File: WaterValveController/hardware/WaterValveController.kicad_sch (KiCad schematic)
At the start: 43 parts, among them J1 12V DC IN, J2 VALVE POWER, J3 RELAY MODULE, J4 FLOW SENSOR, J5 REMOTE RX, J6 ESP, K1 Relay module, SW1 MODE / CAL, U1 L7805 or R-78E5.0-1.0

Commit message: Switch remote to the RX480E logic-output receiver; add PCB prep parts
The 433 MHz receiver is an RX480E-4 module with 5 V logic outputs, not a
relay board. Firmware now defaults to active-high remote inputs. On the
board it plugs into a 7-pin socket powered from filtered 5 V (10R + 47uF
+ 100nF), with 1k series resistors and 100k pull-downs on D0-D3. The old
12 V screw terminal for the remote is gone.

Also adds a 100uF bulk capacitor at the relay header and four M3
mounting holes, renumbers the ESP header to J5 and the Nano decoupling
capacitor to C11, and drops the EasyEDA notes in favour of KiCad.

Co-Authored-By: Claude Opus 5.5 <noreply@anthropic.com>
Claude-Session: https://claude.ai/code/session_01AqRGusXgpSip5brBmMU9hY
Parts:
- removed C10, C12, C8: 100nF, Capacitor_THT:C_Disc_D5.0mm_W2.5mm_P5.00mm, symbol Device:C
- removed J5: REMOTE RX, TerminalBlock_Phoenix:TerminalBlock_Phoenix_MKDS-1,5-6-5.08_1x06_P5.08mm_Horizontal, symbol Connector:Screw_Terminal_01x06
- removed J6: ESP, Connector_PinHeader_2.54mm:PinHeader_1x03_P2.54mm_Vertical, symbol Connector_Generic:Conn_01x03
- removed RX1: 433 MHz 4-ch receiver (momentary), symbol WaterValve:RF_Receiver_4CH
- added C10: 100uF 16V, Capacitor_THT:CP_Radial_D6.3mm_P2.50mm, symbol Device:C_Polarized
- added C8: 47uF 16V, Capacitor_THT:CP_Radial_D5.0mm_P2.00mm, symbol Device:C_Polarized
- added H1, H2, H3, H4: M3, MountingHole:MountingHole_3.2mm_M3, symbol Mechanical:MountingHole
- added J5: ESP, Connector_PinHeader_2.54mm:PinHeader_1x03_P2.54mm_Vertical, symbol Connector_Generic:Conn_01x03
- added R13, R14, R15, R16: 100k, Resistor_THT:R_Axial_DIN0207_L6.3mm_D2.5mm_P10.16mm_Horizontal, symbol Device:R
- added R17: 10R, Resistor_THT:R_Axial_DIN0207_L6.3mm_D2.5mm_P10.16mm_Horizontal, symbol Device:R
- added U2: RX480E-4, Connector_PinSocket_2.54mm:PinSocket_1x07_P2.54mm_Vertical, symbol WaterValve:RX480E
- R10, R7, R8, R9: value 10k -> 1k
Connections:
- net +5V: now also C11.1, C10.1, J5.1 (Pin_1), R17.1; no longer R10.1, R7.1, R8.1, R9.1
- net ESP_DATA: now also J5.2 (Pin_2)
- net GND: now also C10.2, C8.2, J5.3 (Pin_3), R13.2, R14.2, R15.2, R16.2, U2.1 (GND)
- net RF1: now also R13.1
- net RF2: now also R14.1; no longer C9.1
- net RF3: now also R15.1
- net RF4: now also R16.1; no longer C11.1
- new net: C8.1, C9.1, R17.2, U2.2 (+V)
- new net RX_D0: R7.1, U2.3 (D0)
- new net RX_D1: R8.1, U2.4 (D1)
- new net RX_D2: R9.1, U2.5 (D2)
- new net RX_D3: R10.1, U2.6 (D3)
- no-connect marks 17 -> 18
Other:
- note added: "1. D2 flyback diode right at the valve terminals (stripe to +). 2. Valve current has its own pair (J2) back to J1: star ground at J1. 3. Decoupling: C1 + C2 on 12 V, C3 + C4 at U1, C10 at J3, C11 at the Nano, C6 at J4. 4. Flow input: R1 10k pull-up, R2 1k + C5 10nF filter, firmware glitch filter. 5. Button: R3 10k + C7 100nF. Remote: R7-R10 1k series, R13-R16 100k pull-downs, receiver supply filt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"
- note added: "J2: run the valve +12 V and return as their own pair, and keep them away from the sensor cable. Place J1 and J2 side by side. C10 sits at J3 to steady 5 V when the relay coil switches."
- note added: "MOUNTING HOLES (M3)"
- note added: "OFF-BOARD WIRING (connects to J2-J4; not placed on the PCB)"
- note added: "REMOTE RECEIVER (RX480E 433 MHz module, plugs into the board)"
- note added: "U2 plugs into a 7-pin socket. Check that the labels on the back of your module read GND, +V, D0, D1, D2, D3, VT in that order before ordering the PCB. Pair the remote in MOMENTARY mode. Keep the antenna clear of the relay, valve wires and metal."
- note removed: "1. D2 flyback diode right at the valve terminals (stripe to +). 2. Valve current has its own wire pair (J2) back to J1: star ground at J1. 3. Decoupling: C1 + C2 on 12 V, C3 + C4 at U1, C12 at the Nano, C6 at J4. 4. Flow input: R1 10k pull-up, R2 1k + C5 10nF filter, firmware glitch filter. 5. Button and remote inputs: 10k pull-ups + 100nF, firmware debounce. 6. F1 fuse + D1 crowbar protect again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"
- note removed: "J2: run the valve +12 V and return as their own pair, and keep them away from the sensor and remote cables."
- note removed: "OFF-BOARD WIRING (connects to J2-J5; these parts are not placed on the PCB)"
- note removed: "REMOTE RECEIVER INPUTS (433 MHz, 4 relay channels)"
- note removed: "Remote: all COM terminals to GND, NO1-NO4 to J5 pins 3-6. +12 V board shown; power a 5 V board from +5V instead."

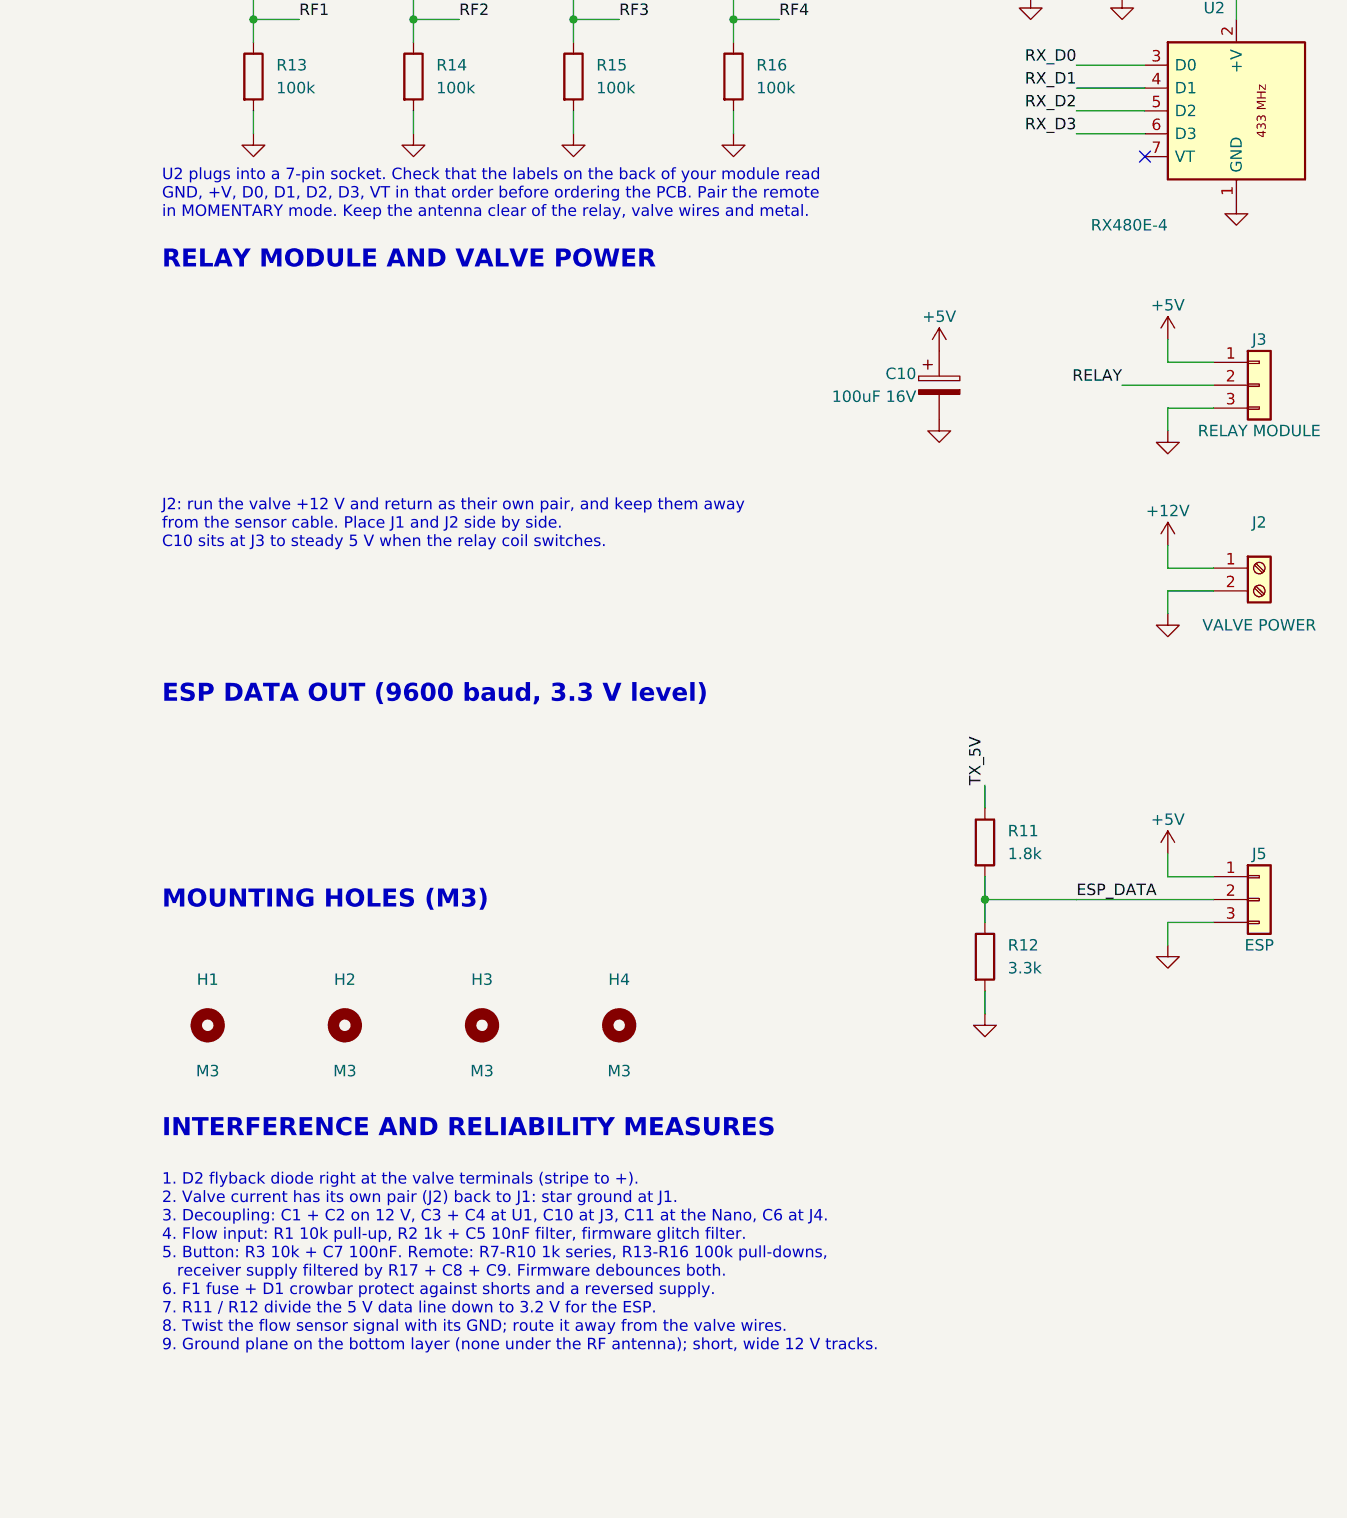
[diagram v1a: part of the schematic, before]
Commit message: Confirm RX480E pin order and mark socket orientation
The module's back labels (RX480R_4CH V4) run GND, +V, D0, D1, D2, D3, VT
from the learn-button end to the antenna end, matching the U2 socket.
Notes now say to mark both socket ends on the silkscreen, since the
upright module would also fit backwards, and the antenna advice covers
an upright module.

Co-Authored-By: Claude Opus 5.5 <noreply@anthropic.com>
Claude-Session: https://claude.ai/code/session_01AqRGusXgpSip5brBmMU9hY
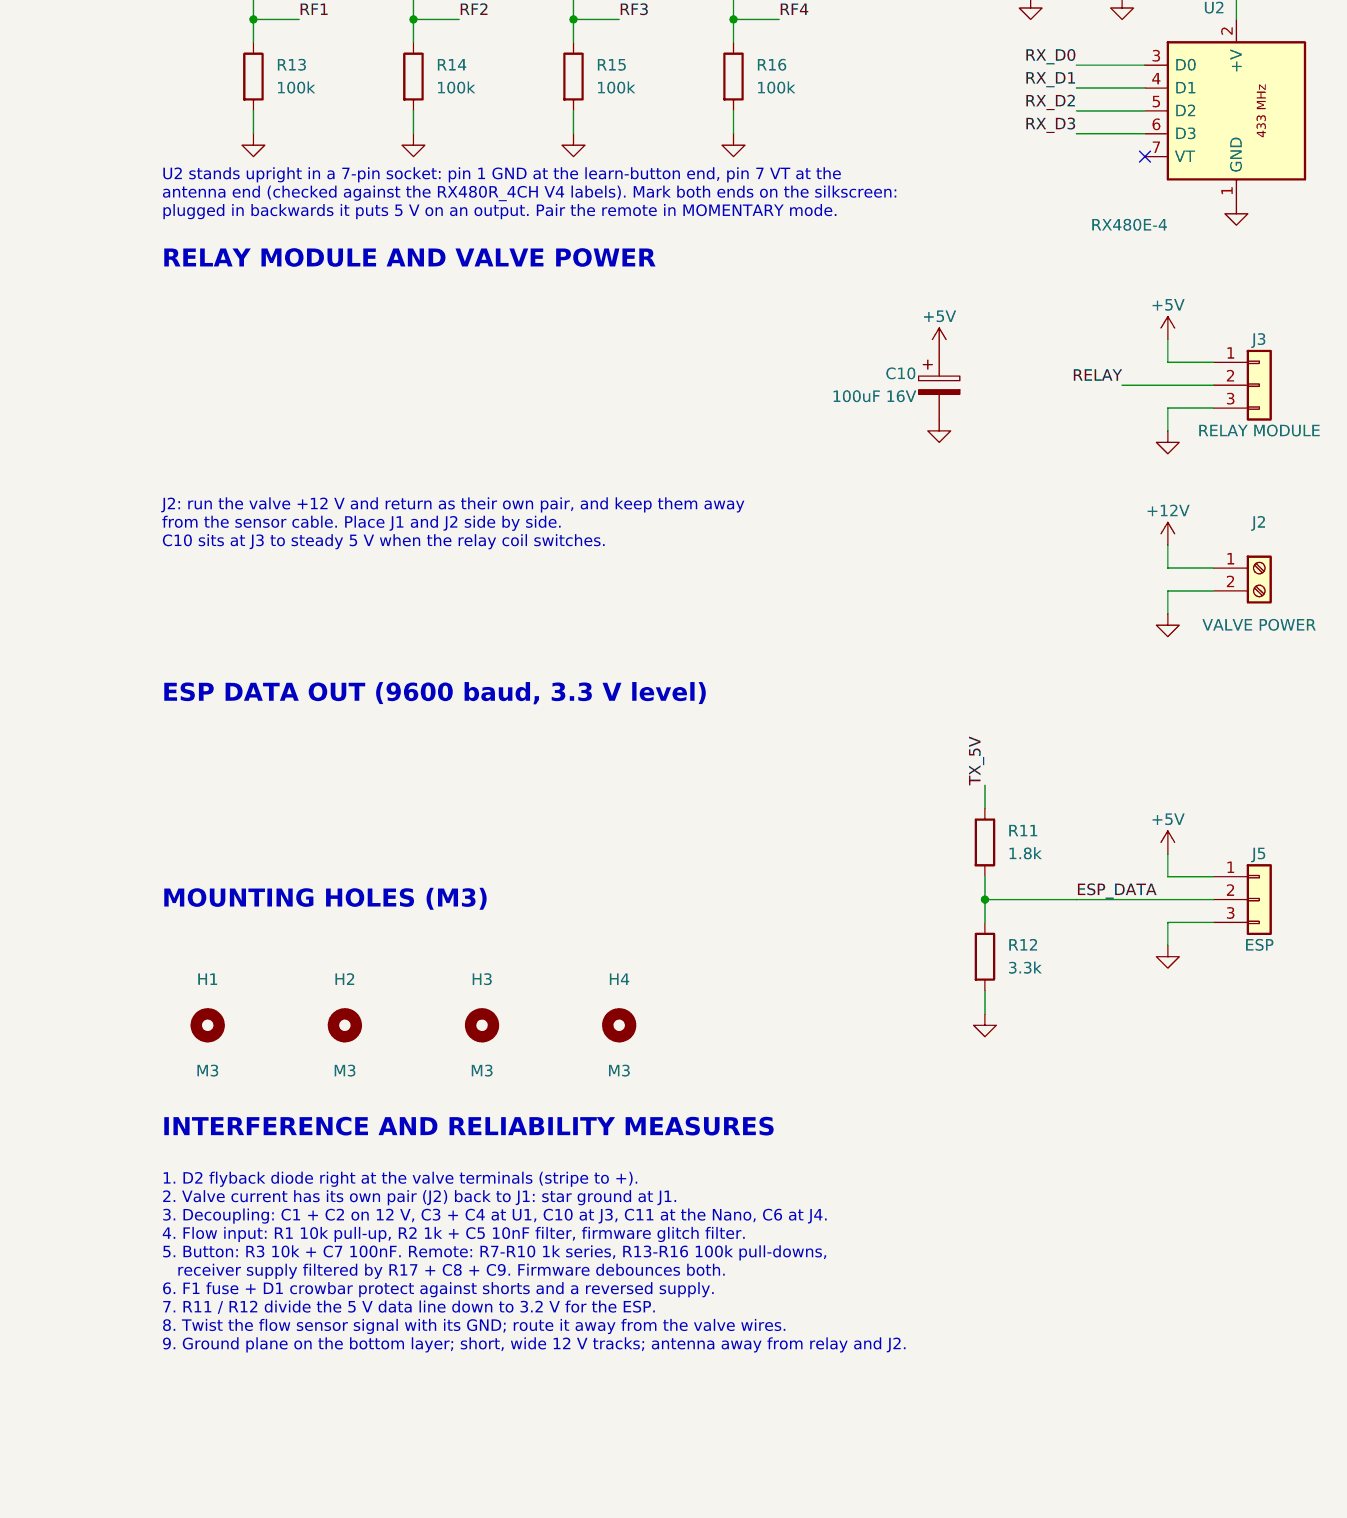
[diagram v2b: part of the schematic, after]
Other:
- note added: "U2 stands upright in a 7-pin socket: pin 1 GND at the learn-button end, pin 7 VT at the antenna end (checked against the RX480R_4CH V4 labels). Mark both ends on the silkscreen: plugged in backwards it puts 5 V on an output. Pair the remote in MOMENTARY mode."
- note removed: "U2 plugs into a 7-pin socket. Check that the labels on the back of your module read GND, +V, D0, D1, D2, D3, VT in that order before ordering the PCB. Pair the remote in MOMENTARY mode. Keep the antenna clear of the relay, valve wires and metal."
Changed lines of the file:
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@@
   (junction (at 342.9 53.34) (diameter 0) (color 0 0 0 0)
   )
-  (text "U2 plugs into a 7-pin socket. Check that the labels on the back of your module read\nGND, +V, D0, D1, D2, D3, VT in that order before ordering the PCB. Pair the remote\nin MOMENTARY mode. Keep the antenna clear of the relay, valve wires and metal." (at 279.4 70 0)
+  (text "U2 stands upright in a 7-pin socket: pin 1 GND at the learn-button end, pin 7 VT at the\nantenna end (checked against the RX480R_4CH V4 labels). Mark both ends on the silkscreen:\nplugged in backwards it puts 5 V on an output. Pair the remote in MOMENTARY mode." (at 279.4 70 0)
     (effects (font (size 1.27 1.27)) (justify left top))
   )
@@
     (effects (font (size 2 2) bold) (justify left bottom))
   )
-  (text "1. D2 flyback diode right at the valve terminals (stripe to +).\n2. Valve current has its own pair (J2) back to J1: star ground at J1.\n3. Decoupling: C1 + C2 on 12 V, C3 + C4 at U1, C10 at J3, C11 at the Nano, C6 at J4.\n4. Flow input: R1 10k pull-up, R2 1k + C5 10nF filter, firmware glitch filter.\n5. Button: R3 10k + C7 100nF. Remote: R7-R10 1k series, R13-R16 100k pull-downs,\n   receiver supply filtered by R17 + C8 + C9. Firmware debounces both.\n6. F1 fuse + D1 crowbar protect against shorts and a reversed supply.\n7. R11 / R12 divide the 5 V data line down to 3.2 V for the ESP.\n8. Twist the flow sensor signal with its GND; route it away from the valve wires.\n9. Ground plane on the bottom layer (none under the RF antenna); short, wide 12 V tracks." (at 279.4 181.61 0)
+  (text "1. D2 flyback diode right at the valve terminals (stripe to +).\n2. Valve current has its own pair (J2) back to J1: star ground at J1.\n3. Decoupling: C1 + C2 on 12 V, C3 + C4 at U1, C10 at J3, C11 at the Nano, C6 at J4.\n4. Flow input: R1 10k pull-up, R2 1k + C5 10nF filter, firmware glitch filter.\n5. Button: R3 10k + C7 100nF. Remote: R7-R10 1k series, R13-R16 100k pull-downs,\n   receiver supply filtered by R17 + C8 + C9. Firmware debounces both.\n6. F1 fuse + D1 crowbar protect against shorts and a reversed supply.\n7. R11 / R12 divide the 5 V data line down to 3.2 V for the ESP.\n8. Twist the flow sensor signal with its GND; route it away from the valve wires.\n9. Ground plane on the bottom layer; short, wide 12 V tracks; antenna away from relay and J2." (at 279.4 181.61 0)
     (effects (font (size 1.27 1.27)) (justify left top))
   )

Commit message: Document the ESP32-C3-Zero on the ESP header
J5 stays a 3-pin header (5V, DATA, GND). Notes now name the Waveshare
ESP32-C3-Zero: 5V to its 5V pin, DATA to GPIO20, and why the R11/R12
divider stays (its GPIOs are 3.3 V only). The switching regulator is now
the recommended U1, since the ESP's Wi-Fi peaks take the 5 V load to
about 0.5 A.

Co-Authored-By: Claude Opus 5.5 <noreply@anthropic.com>
Claude-Session: https://claude.ai/code/session_01AqRGusXgpSip5brBmMU9hY
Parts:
- J5: value ESP -> ESP32-C3
- U1: value L7805 or R-78E5.0-1.0 -> R-78E5.0-1.0 or L7805
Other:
- note added: "ESP32-C3-Zero: J5 5V -> 5V pin, DATA -> GPIO20 (RX), GND -> GND. Its GPIOs are 3.3 V only, so R11 / R12 drop the Nano's 5 V data to 3.2 V."
- note added: "F1 + D1: if the supply is connected backwards, D1 conducts and blows F1. U1: the ESP32-C3 Wi-Fi peaks take the 5 V load to about 0.5 A. Use a pin-compatible switching regulator (e.g. R-78E5.0-1.0) or a 5 V buck module wired to IN / GND / OUT. An L7805 needs a heatsink."
- note removed: "F1 + D1: if the supply is connected backwards, D1 conducts and blows F1. U1: L7805 needs a small heatsink. Once an ESP is fitted, use a pin-compatible switching regulator (e.g. R-78E5.0-1.0) or a 5 V buck module wired to IN / GND / OUT."
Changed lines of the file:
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@@
       (effects (font (size 1.27 1.27)))
     )
-    (property "Value" "L7805 or R-78E5.0-1.0" (at 109.22 46.99 0)
+    (property "Value" "R-78E5.0-1.0 or L7805" (at 109.22 46.99 0)
       (effects (font (size 1.27 1.27)))
     )
@@
     )
   )
-  (text "F1 + D1: if the supply is connected backwards, D1 conducts and blows F1.\nU1: L7805 needs a small heatsink. Once an ESP is fitted, use a pin-compatible\nswitching regulator (e.g. R-78E5.0-1.0) or a 5 V buck module wired to IN / GND / OUT." (at 20.32 72.39 0)
+  (text "F1 + D1: if the supply is connected backwards, D1 conducts and blows F1.\nU1: the ESP32-C3 Wi-Fi peaks take the 5 V load to about 0.5 A. Use a pin-compatible switching\nregulator (e.g. R-78E5.0-1.0) or a 5 V buck module wired to IN / GND / OUT. An L7805 needs a heatsink." (at 20.32 72.39 0)
     (effects (font (size 1.27 1.27)) (justify left top))
   )
@@
     (effects (font (size 2 2) bold) (justify left bottom))
   )
+  (text "ESP32-C3-Zero: J5 5V -> 5V pin, DATA -> GPIO20 (RX),\nGND -> GND. Its GPIOs are 3.3 V only, so R11 / R12\ndrop the Nano's 5 V data to 3.2 V." (at 279.4 134.62 0)
+    (effects (font (size 1.27 1.27)) (justify left top))
+  )
   (wire (pts (xy 370.84 138.43) (xy 370.84 140.97))
     (stroke (width 0) (type default))
@@
       (effects (font (size 1.27 1.27)))
     )
-    (property "Value" "ESP" (at 401.32 156.21 0)
-      (effects (font (size 1.27 1.27)))
-    )
+    (property "Value" "ESP32-C3" (at 401.32 156.21 0)
+      (effects (font (size 1.27 1.27)))
+    )
